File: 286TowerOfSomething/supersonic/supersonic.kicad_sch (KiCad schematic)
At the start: 1 part, among them J1 Bus_ISA_8bit

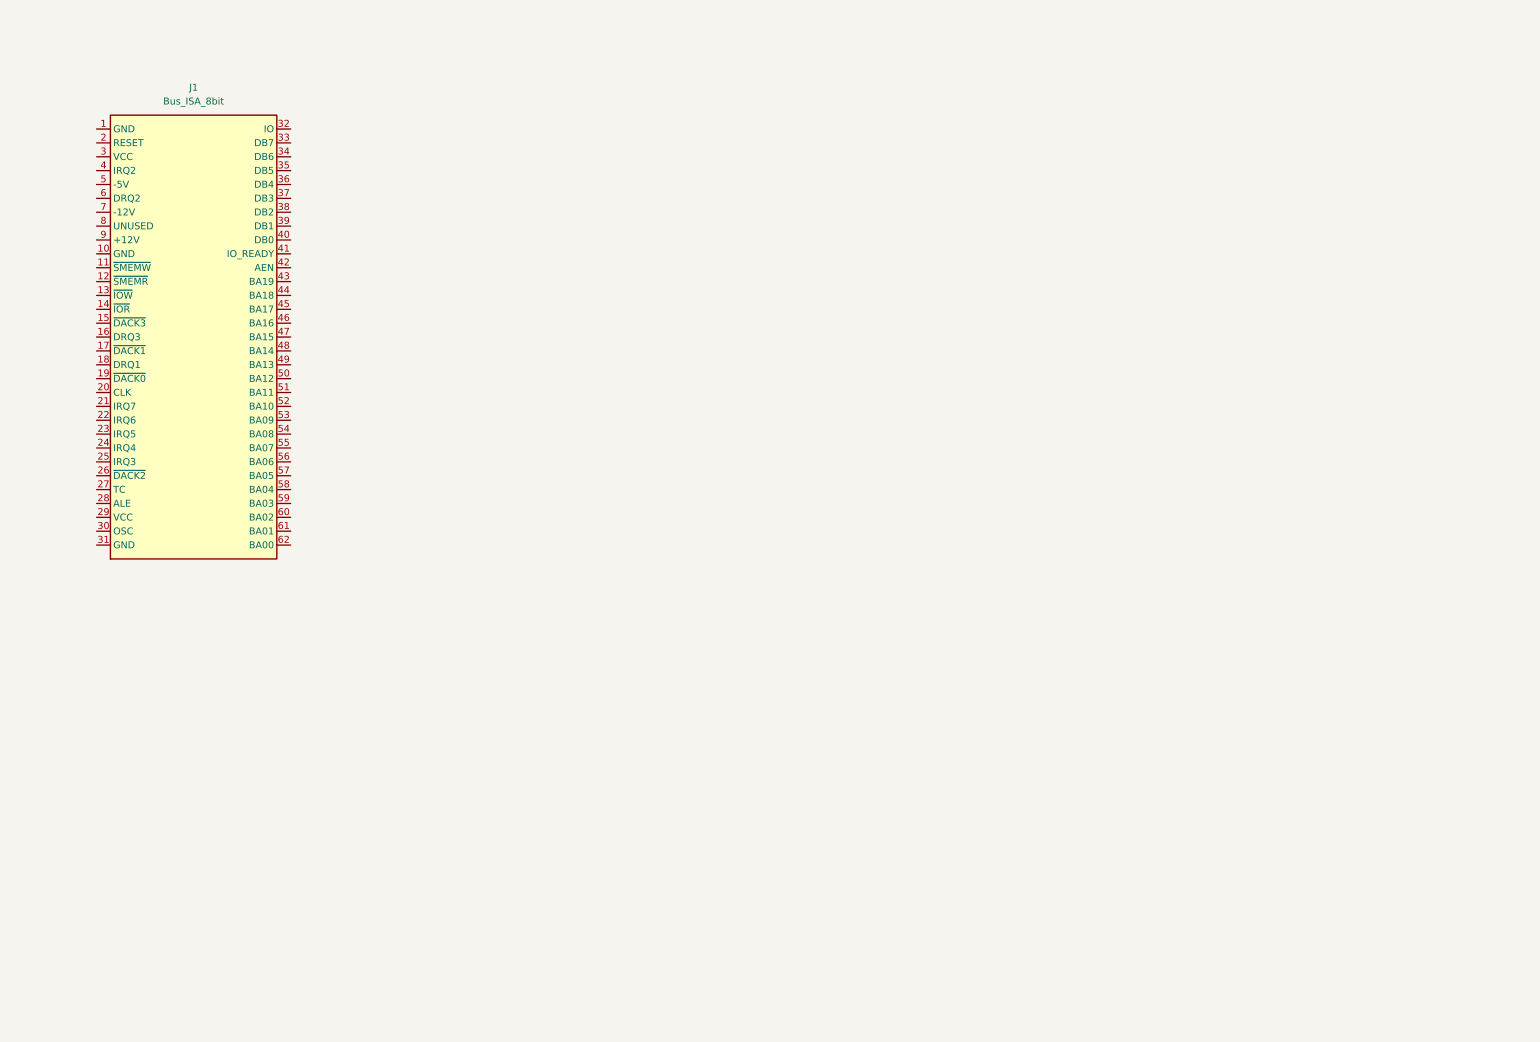
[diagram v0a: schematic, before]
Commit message: Started on schematic for sound card
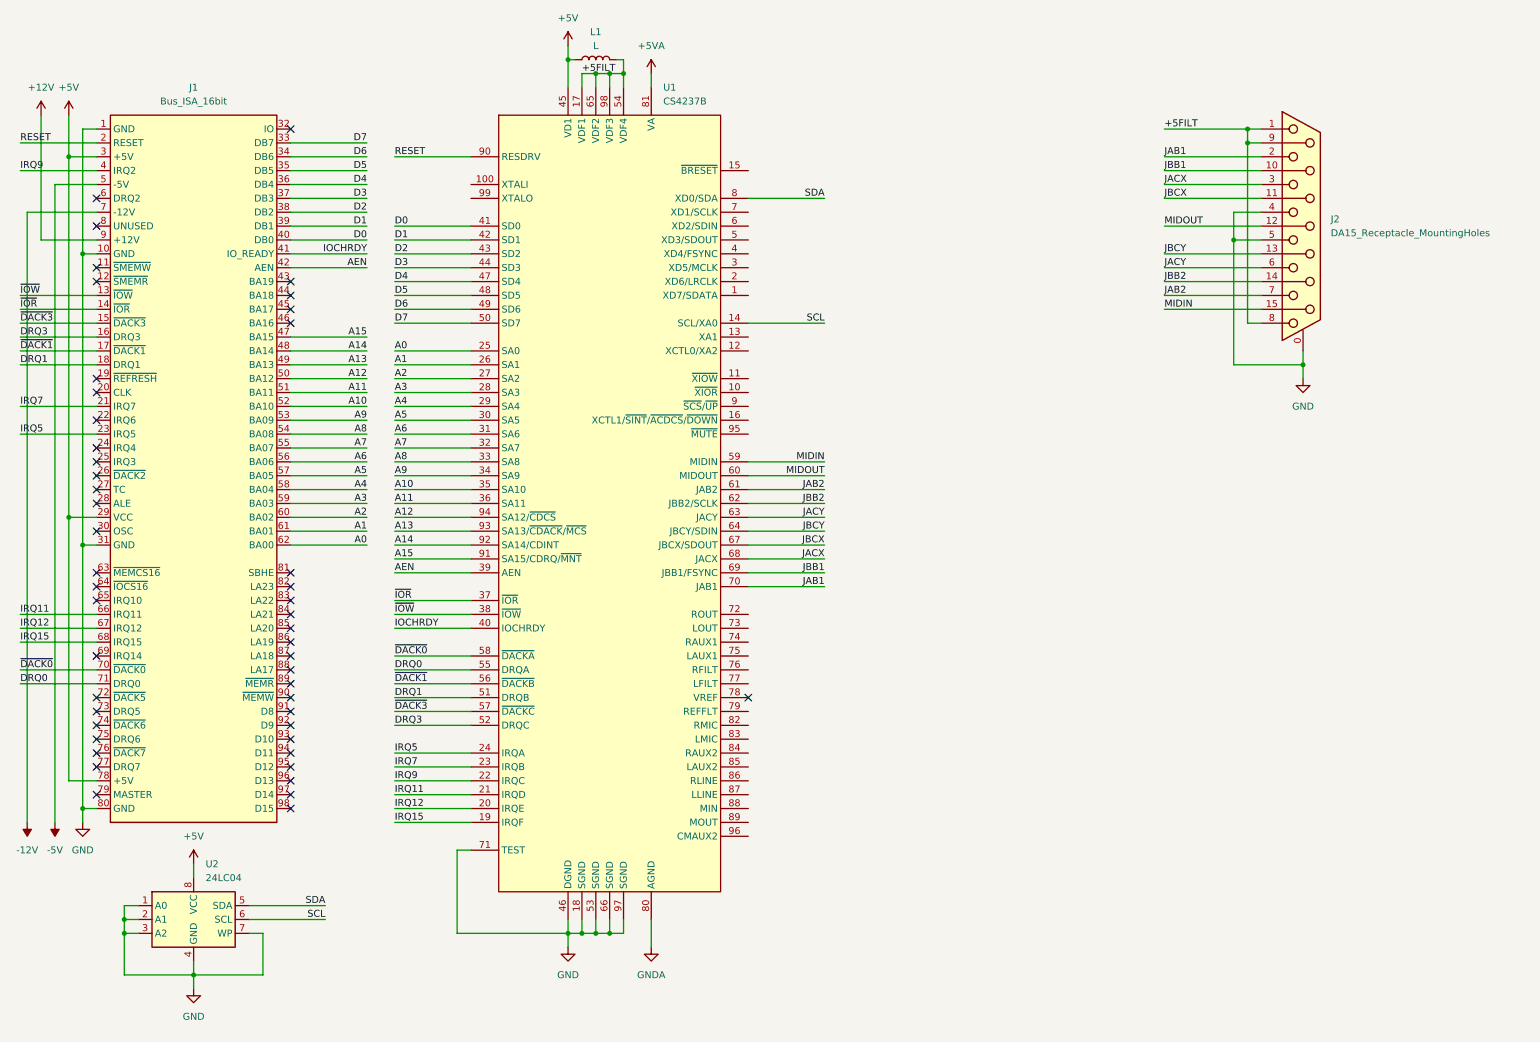
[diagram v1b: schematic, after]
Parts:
- removed J1: Bus_ISA_8bit, pc-parts:BUS_AT_8BIT, symbol Connector:Bus_ISA_8bit
- added J1: Bus_ISA_16bit, symbol Connector:Bus_ISA_16bit
- added J2: DA15_Receptacle_MountingHoles, symbol Connector:DA15_Receptacle_MountingHoles
- added L1: L, symbol Device:L
- added U1: CS4237B, Package_QFP:LQFP-100_14x14mm_P0.5mm, symbol pc-parts:CS4237B
- added U2: 24LC04, symbol Memory_EEPROM:24LC04
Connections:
- new net +12V: J1.9 (+12V)
- new net +5FILT: J2.1, J2.8, J2.9 (P9), L1.2, U1.17 (VDF1), U1.54 (VDF4), U1.65 (VDF2), U1.98 (VDF3)
- new net +5V: J1.29 (VCC), J1.3 (+5V), J1.78 (+5V), L1.1, U1.45 (VD1), U2.8 (VCC)
- new net +5VA: U1.81 (VA)
- new net -12V: J1.7 (-12V)
- new net -5V: J1.5 (-5V)
- new net A0: J1.62 (BA00), U1.25 (SA0)
- new net A1: J1.61 (BA01), U1.26 (SA1)
- new net A10: J1.52 (BA10), U1.35 (SA10)
- new net A11: J1.51 (BA11), U1.36 (SA11)
- new net A12: J1.50 (BA12), U1.94 (SA12/~{CDCS})
- new net A13: J1.49 (BA13), U1.93 (SA13/~{CDACK}/~{MCS})
- new net A14: J1.48 (BA14), U1.92 (SA14/CDINT)
- new net A15: J1.47 (BA15), U1.91 (SA15/CDRQ/~{MNT})
- new net A2: J1.60 (BA02), U1.27 (SA2)
- new net A3: J1.59 (BA03), U1.28 (SA3)
- new net A4: J1.58 (BA04), U1.29 (SA4)
- new net A5: J1.57 (BA05), U1.30 (SA5)
- new net A6: J1.56 (BA06), U1.31 (SA6)
- new net A7: J1.55 (BA07), U1.32 (SA7)
- new net A8: J1.54 (BA08), U1.33 (SA8)
- new net A9: J1.53 (BA09), U1.34 (SA9)
- new net AEN: J1.42 (AEN), U1.39 (AEN)
- new net D0: J1.40 (DB0), U1.41 (SD0)
- new net D1: J1.39 (DB1), U1.42 (SD1)
- new net D2: J1.38 (DB2), U1.43 (SD2)
- new net D3: J1.37 (DB3), U1.44 (SD3)
- new net D4: J1.36 (DB4), U1.47 (SD4)
- new net D5: J1.35 (DB5), U1.48 (SD5)
- new net D6: J1.34 (DB6), U1.49 (SD6)
- new net D7: J1.33 (DB7), U1.50 (SD7)
- new net DRQ0: J1.71 (DRQ0), U1.55 (DRQA)
- new net DRQ1: J1.18 (DRQ1), U1.51 (DRQB)
- new net DRQ3: J1.16 (DRQ3), U1.52 (DRQC)
- new net GND: J1.1 (GND), J1.10 (GND), J1.31 (GND), J1.80 (GND), J2.0 (PAD), J2.4, J2.5, U1.18 (SGND), U1.46 (DGND), U1.53 (SGND), U1.66 (SGND), U1.71 (TEST), U1.97 (SGND), U2.1 (A0), U2.2 (A1), U2.3 (A2), U2.4 (GND), U2.7 (WP)
- new net GNDA: U1.80 (AGND)
- new net IOCHRDY: J1.41 (IO_READY), U1.40 (IOCHRDY)
- new net IRQ11: J1.66 (IRQ11), U1.21 (IRQD)
- new net IRQ12: J1.67 (IRQ12), U1.20 (IRQE)
- new net IRQ15: J1.68 (IRQ15), U1.19 (IRQF)
- new net IRQ5: J1.23 (IRQ5), U1.24 (IRQA)
- new net IRQ7: J1.21 (IRQ7), U1.23 (IRQB)
- new net IRQ9: J1.4 (IRQ2), U1.22 (IRQC)
- new net JAB1: J2.2, U1.70 (JAB1)
- new net JAB2: J2.7, U1.61 (JAB2)
- new net JACX: J2.3, U1.68 (JACX)
- new net JACY: J2.6, U1.63 (JACY)
- new net JBB1: J2.10 (P10), U1.69 (JBB1/FSYNC)
- new net JBB2: J2.14 (P14), U1.62 (JBB2/SCLK)
- new net JBCX: J2.11 (P111), U1.67 (JBCX/SDOUT)
- new net JBCY: J2.13 (P13), U1.64 (JBCY/SDIN)
- new net MIDIN: J2.15 (P15), U1.59 (MIDIN)
- new net MIDOUT: J2.12 (P12), U1.60 (MIDOUT)
- new net RESET: J1.2 (RESET), U1.90 (RESDRV)
- new net SCL: U1.14 (SCL/XA0), U2.6 (SCL)
- new net SDA: U1.8 (XD0/SDA), U2.5 (SDA)
- new net ~{DACK0}: J1.70 (~{DACK0}), U1.58 (~{DACKA})
- new net ~{DACK1}: J1.17 (~{DACK1}), U1.56 (~{DACKB})
- new net ~{DACK3}: J1.15 (~{DACK3}), U1.57 (~{DACKC})
- new net ~{IOR}: J1.14 (~{IOR}), U1.37 (~{IOR})
- new net ~{IOW}: J1.13 (~{IOW}), U1.38 (~{IOW})
- no-connect marks 0 -> 48

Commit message: Adding template to sound card:
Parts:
- added BRACKET1: ~, pc-parts:PC_BRACKET_ISA_KEYSTONE_9202_Rev1, symbol pc-parts:9202
- J1: footprint (none) -> Connector_PCBEdge:BUS_AT
- J2: footprint (none) -> Connector_Dsub:DSUB-15_Female_Horizontal_P2.77x2.84mm_EdgePinOffset4.94mm_Housed_MountingHolesOffset4.94mm
- U2: footprint (none) -> Package_DIP:DIP-8_W7.62mm
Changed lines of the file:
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@@
 			)
 		)
-		(property "Footprint" ""
+		(property "Footprint" "Package_DIP:DIP-8_W7.62mm"
 			(at 50.8 177.8 0)
 			(effects
@@
 			)
 		)
-		(property "Footprint" ""
+		(property "Footprint" "Connector_PCBEdge:BUS_AT"
 			(at 50.8 95.25 0)
 			(effects
@@
 	)
 	(symbol
+		(lib_id "pc-parts:9202")
+		(at 149.86 196.85 0)
+		(unit 1)
+		(exclude_from_sim no)
+		(in_bom yes)
+		(on_board yes)
+		(dnp no)
+		(fields_autoplaced yes)
+		(property "Reference" "BRACKET1"
+			(at 149.86 196.85 0)
+			(effects
+				(font
+					(size 1.27 1.27)
+				)
+				(hide yes)
+			)
+		)
+		(property "Value" "~"
+			(at 154.94 196.85 0)
+			(effects
+				(font
+					(size 1.27 1.27)
+				)
+				(justify left)
+			)
+		)
+		(property "Footprint" "pc-parts:PC_BRACKET_ISA_KEYSTONE_9202_Rev1"
+			(at 149.86 196.85 0)
+			(effects
+				(font
+					(size 1.27 1.27)
+				)
+				(hide yes)
+			)
+		)
+		(property "Datasheet" ""
+			(at 149.86 196.85 0)
+			(effects
+				(font
+					(size 1.27 1.27)
+				)
+				(hide yes)
+			)
+		)
+		(property "Description" ""
+			(at 149.86 196.85 0)
+			(effects
+				(font
+					(size 1.27 1.27)
+				)
+				(hide yes)
+			)
+		)
+		(instances
+			(project ""
+				(path "/8ef5b5fc-79fc-41ed-83d5-69b0cc357958"
+					(reference "BRACKET1")
+					(unit 1)
+				)
+			)
+		)
+	)
+	(symbol
 		(lib_id "power:GND")
 		(at 30.48 160.02 0)
@@
 			)
 		)
-		(property "Footprint" ""
+		(property "Footprint" "Connector_Dsub:DSUB-15_Female_Horizontal_P2.77x2.84mm_EdgePinOffset4.94mm_Housed_MountingHolesOffset4.94mm"
 			(at 254 50.8 0)
 			(effects
